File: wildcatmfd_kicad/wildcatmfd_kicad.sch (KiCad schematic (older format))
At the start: 2 parts

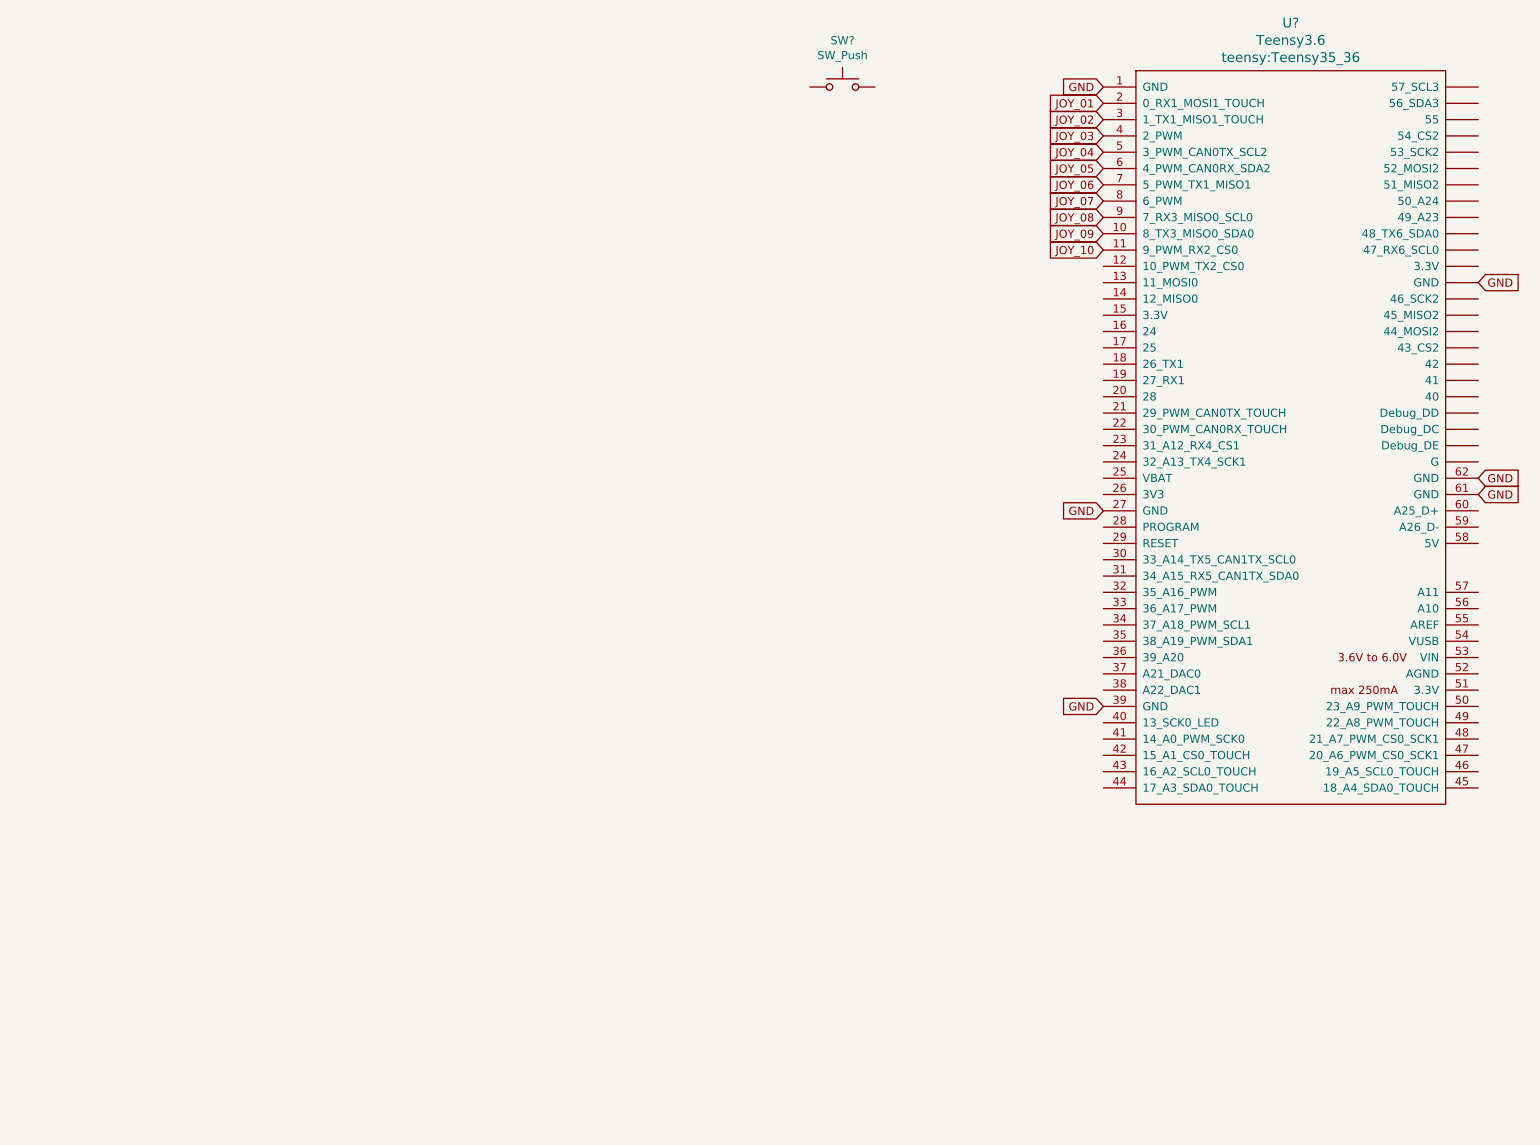
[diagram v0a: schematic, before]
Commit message: Schematic done
Need to design the board layout now
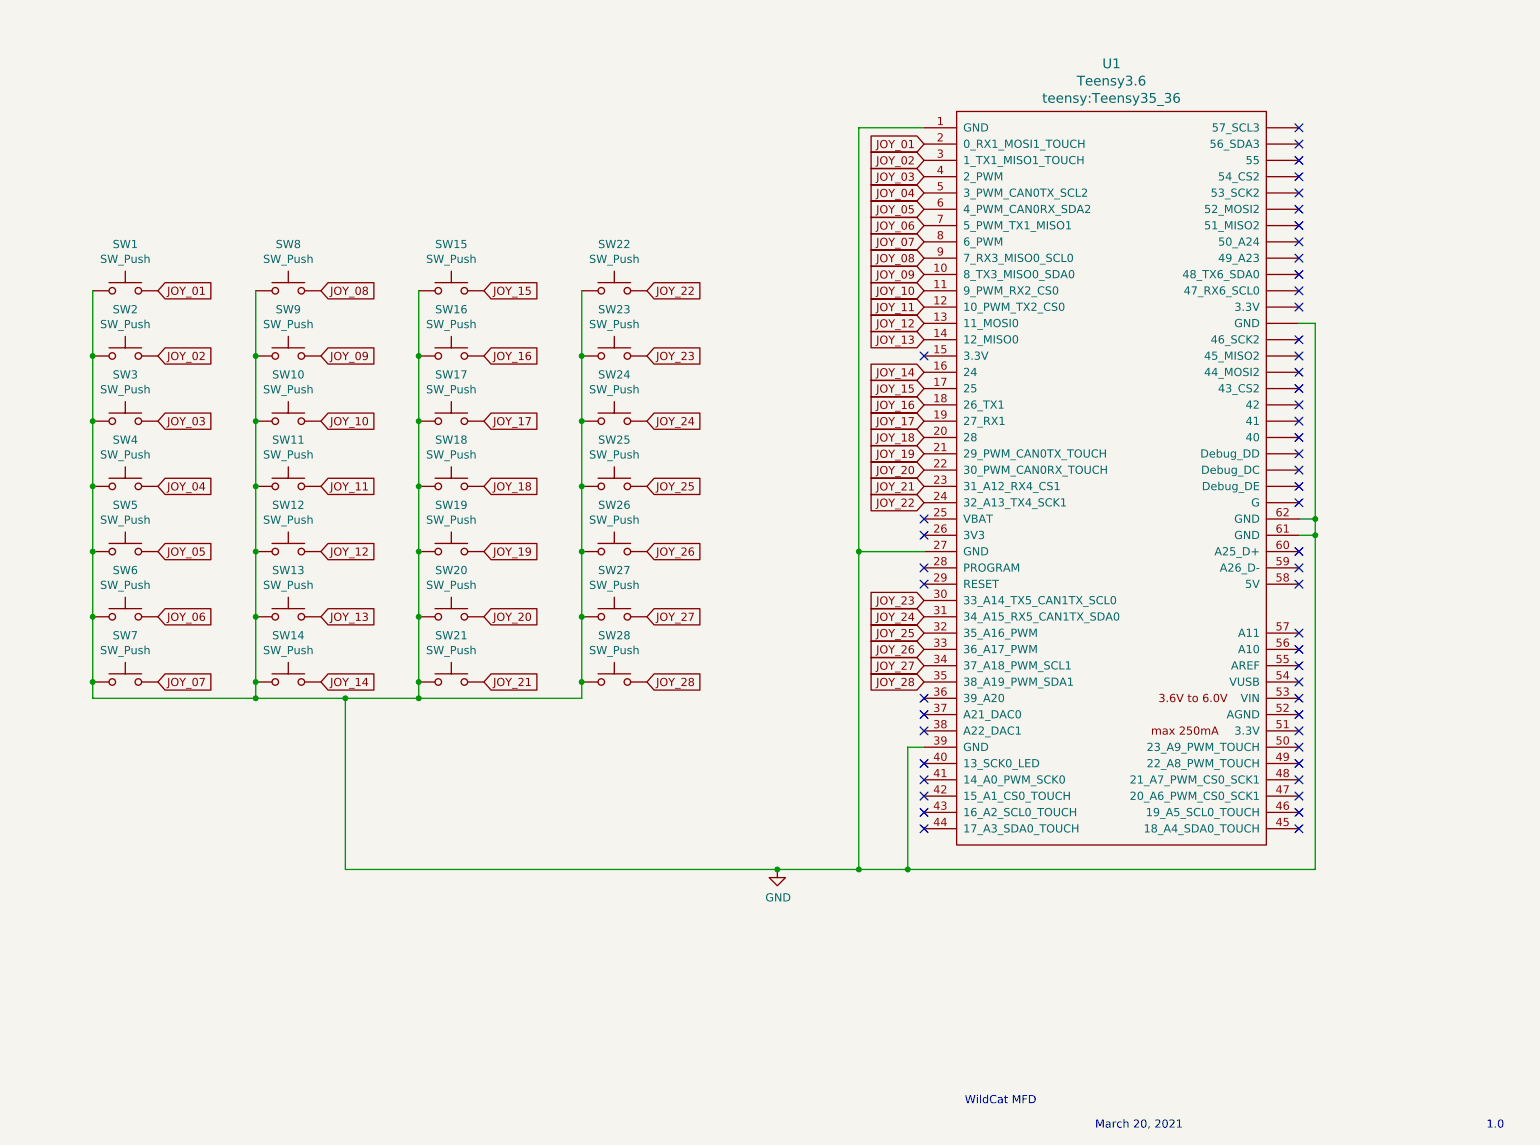
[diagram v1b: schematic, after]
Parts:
- added SW1, SW10, SW11, SW12, SW13, SW14, SW15, SW16, SW17, SW18, SW19, SW2, SW20, SW21, SW23, SW24, SW25, SW26, SW27, SW28, SW3, SW4, SW5, SW6, SW7, SW8, SW9: SW_Push, Button_Switch_Keyboard:SW_Cherry_MX_1.00u_PCB, symbol Switch:SW_Push
- gave numbers to parts that had none: 2
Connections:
- net GND: now also SW22.1, SW1.1, SW10.1, SW11.1, SW12.1, SW13.1, SW14.1, SW15.1, SW16.1, SW17.1, SW18.1, SW19.1, SW2.1, SW20.1, SW21.1, SW23.1, SW24.1, SW25.1, SW26.1, SW27.1, SW28.1, SW3.1, SW4.1, SW5.1, SW6.1, SW7.1, SW8.1, SW9.1
- net JOY_01: now also SW1.2
- net JOY_02: now also SW2.2
- net JOY_03: now also SW3.2
- net JOY_04: now also SW4.2
- net JOY_05: now also SW5.2
- net JOY_06: now also SW6.2
- net JOY_07: now also SW7.2
- net JOY_08: now also SW8.2
- net JOY_09: now also SW9.2
- net JOY_10: now also SW10.2
- net JOY_11: now reaches U1.12 (10_PWM_TX2_CS0)
- net JOY_11: now also SW11.2
- net JOY_12: now reaches U1.13 (11_MOSI0)
- net JOY_12: now also SW12.2
- net JOY_13: now reaches U1.14 (12_MISO0)
- net JOY_13: now also SW13.2
- net JOY_14: now reaches U1.16 (24)
- net JOY_14: now also SW14.2
- net JOY_15: now reaches U1.17 (25)
- net JOY_15: now also SW15.2
- net JOY_16: now reaches U1.18 (26_TX1)
- net JOY_16: now also SW16.2
- net JOY_17: now reaches U1.19 (27_RX1)
- net JOY_17: now also SW17.2
- net JOY_18: now reaches U1.20 (28)
- net JOY_18: now also SW18.2
- net JOY_19: now reaches U1.21 (29_PWM_CAN0TX_TOUCH)
- net JOY_19: now also SW19.2
- net JOY_20: now reaches U1.22 (30_PWM_CAN0RX_TOUCH)
- net JOY_20: now also SW20.2
- net JOY_21: now reaches U1.23 (31_A12_RX4_CS1)
- net JOY_21: now also SW21.2
- net JOY_22: now reaches U1.24 (32_A13_TX4_SCK1)
- net JOY_22: now also SW22.2
- net JOY_23: now reaches U1.30 (33_A14_TX5_CAN1TX_SCL0)
- net JOY_23: now also SW23.2
- net JOY_24: now reaches U1.31 (34_A15_RX5_CAN1TX_SDA0)
- net JOY_24: now also SW24.2
- net JOY_25: now reaches U1.32 (35_A16_PWM)
- net JOY_25: now also SW25.2
- net JOY_26: now reaches U1.33 (36_A17_PWM)
- net JOY_26: now also SW26.2
- net JOY_27: now reaches U1.34 (37_A18_PWM_SCL1)
- net JOY_27: now also SW27.2
- net JOY_28: now reaches U1.35 (38_A19_PWM_SDA1)
- net JOY_28: now also SW28.2
- no-connect marks 0 -> 52
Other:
- note added: "1.0"
- note added: "March 20, 2021"
- note added: "WildCat MFD"
- moved on the sheet: SW22, U1

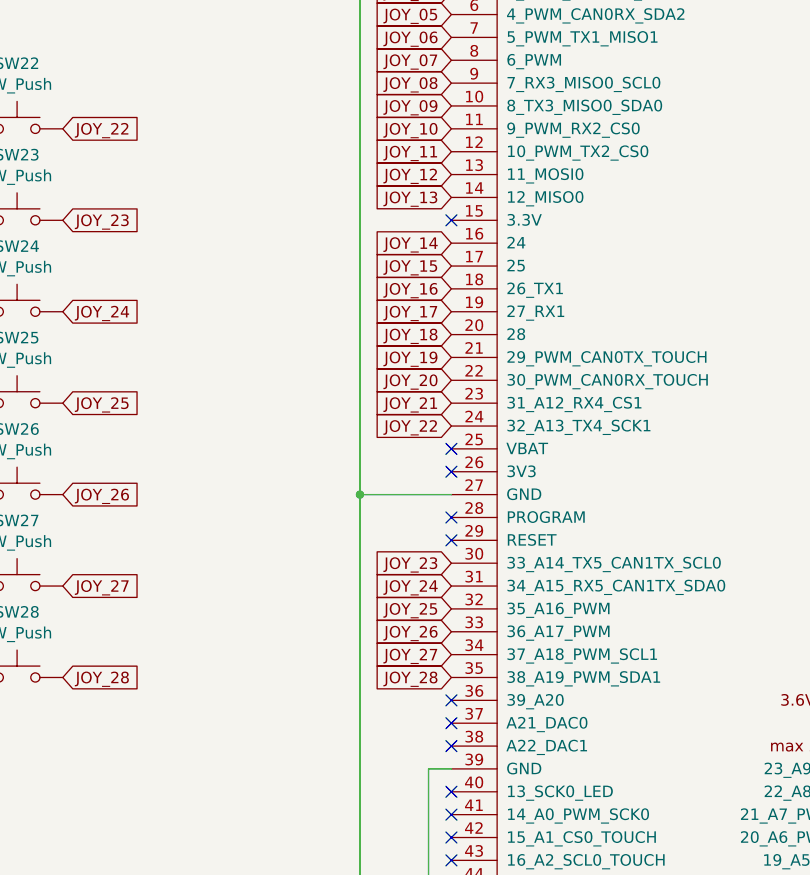
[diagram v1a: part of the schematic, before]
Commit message: Moved JOY_12 off of Pin 13
Pin 13 is the LED on the Teensy, not recommended to be used as an input
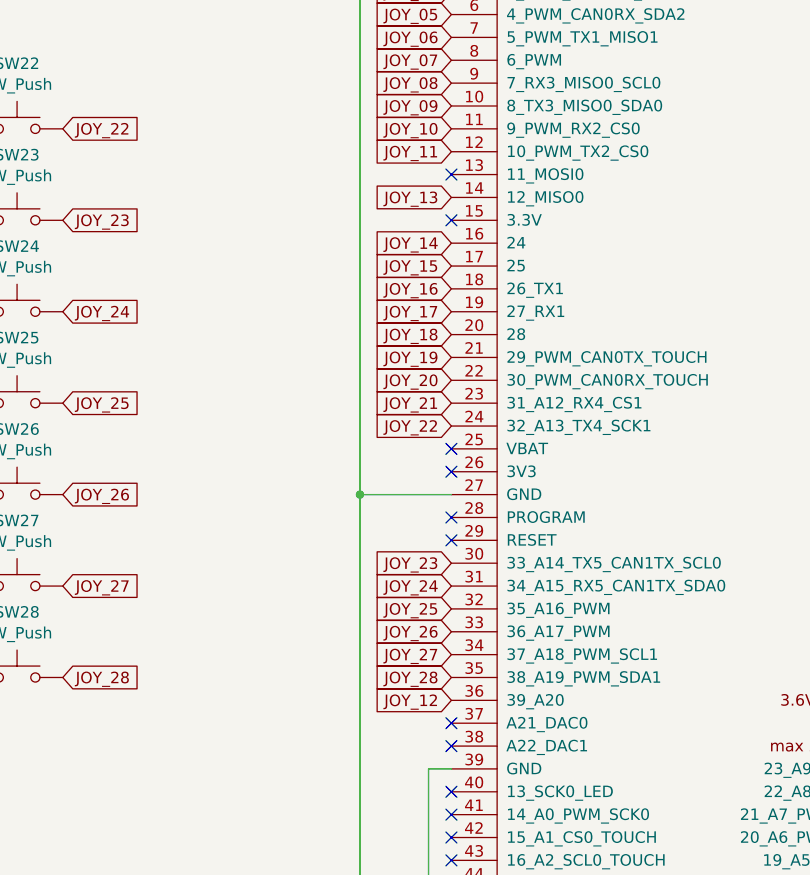
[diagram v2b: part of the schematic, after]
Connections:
- net JOY_12: now also U1.36 (39_A20); no longer U1.13 (11_MOSI0)
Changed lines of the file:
@@
 Text GLabel 7100 2600 0    50   Input ~ 0
 JOY_11
-Text GLabel 7100 2700 0    50   Input ~ 0
+Text GLabel 7100 5000 0    50   Input ~ 0
 JOY_12
 Text GLabel 7100 2800 0    50   Input ~ 0
@@
 NoConn ~ 7100 4200
 NoConn ~ 7100 4300
-NoConn ~ 7100 5000
 NoConn ~ 7100 5100
 NoConn ~ 7100 5200
@@
 Wire Wire Line
 	9500 4000 9500 3900
+NoConn ~ 7100 2700
 $EndSCHEMATC

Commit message: Version 1.0 Complete
Will order PCBs!
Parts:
- removed SW21, SW22, SW23, SW24, SW25, SW26, SW27, SW28: SW_Push, Button_Switch_Keyboard:SW_Cherry_MX_1.00u_PCB, symbol Switch:SW_Push
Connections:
- net JOY_21 is gone; now on net JOY_06: U1.23 (31_A12_RX4_CS1)
- net JOY_22 is gone; now on net JOY_07: U1.24 (32_A13_TX4_SCK1)
- net JOY_23 is gone; now on net JOY_08: U1.30 (33_A14_TX5_CAN1TX_SCL0)
- net JOY_24 is gone; now on net JOY_09: U1.31 (34_A15_RX5_CAN1TX_SDA0)
- net JOY_25 is gone; now on net JOY_10: U1.32 (35_A16_PWM)
- net JOY_26 is gone; now on net JOY_11: U1.33 (36_A17_PWM)
- net JOY_27 is gone; now on net JOY_12: U1.34 (37_A18_PWM_SCL1)
- net JOY_28 is gone; now on net JOY_13: U1.35 (38_A19_PWM_SDA1)
- net JOY_01: now also U1.4 (2_PWM); no longer U1.2 (0_RX1_MOSI1_TOUCH)
- net JOY_02: now also U1.5 (3_PWM_CAN0TX_SCL2); no longer U1.3 (1_TX1_MISO1_TOUCH)
- net JOY_03: now also U1.6 (4_PWM_CAN0RX_SDA2); no longer U1.4 (2_PWM)
- net JOY_04: now also U1.7 (5_PWM_TX1_MISO1); no longer U1.5 (3_PWM_CAN0TX_SCL2)
- net JOY_05: now also U1.8 (6_PWM); no longer U1.6 (4_PWM_CAN0RX_SDA2)
- net JOY_06: no longer U1.7 (5_PWM_TX1_MISO1)
- net JOY_07: no longer U1.8 (6_PWM)
- net JOY_08: no longer U1.9 (7_RX3_MISO0_SCL0)
- net JOY_09: no longer U1.10 (8_TX3_MISO0_SDA0)
- net JOY_10: no longer U1.11 (9_PWM_RX2_CS0)
- net JOY_11: no longer U1.12 (10_PWM_TX2_CS0)
- net JOY_12: no longer U1.36 (39_A20)
- net JOY_13: no longer U1.14 (12_MISO0)
- net JOY_14: now also U1.36 (39_A20); no longer U1.16 (24)
- net JOY_15: now also U1.47 (20_A6_PWM_CS0_SCK1); no longer U1.17 (25)
- net JOY_16: now also U1.48 (21_A7_PWM_CS0_SCK1); no longer U1.18 (26_TX1)
- net JOY_17: now also U1.49 (22_A8_PWM_TOUCH); no longer U1.19 (27_RX1)
- net JOY_18: now also U1.50 (23_A9_PWM_TOUCH); no longer U1.20 (28)
- net JOY_19: now also U1.2 (0_RX1_MOSI1_TOUCH); no longer U1.21 (29_PWM_CAN0TX_TOUCH)
- net JOY_20: now also U1.3 (1_TX1_MISO1_TOUCH); no longer U1.22 (30_PWM_CAN0RX_TOUCH)
- no-connect marks 52 -> 60
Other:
- moved on the sheet: SW1, SW10, SW11, SW12, SW13, SW14, SW15, SW16, SW17, SW18, SW19, SW2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
